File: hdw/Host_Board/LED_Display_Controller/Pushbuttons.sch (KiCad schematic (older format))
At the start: 4 parts

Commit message: Added encoder stuff
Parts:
- added C? (x3): 0.1uF, symbol LED_Display_Local_Library:C_Custom
- added R? (x2): 10k, symbol LED_Display_Local_Library:R_Custom
- added R? (x2): 1k, symbol LED_Display_Local_Library:R_Custom
- added U?: 74LVC2G14, TO_SOT_Packages_SMD:SOT-363_SC-70-6, symbol LED_Display_Local_Library:74LVC2G14_Power
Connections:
- net +3V3: now also C?.1, R?.1, R?.1
- net GND: now also C?.2, C?.2, C?.2
- net at SW?.A: now also R?.2, R?.2
- net at SW?.B: now also R?.2, R?.2
- new net: C?.1, R?.1 (x2)
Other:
- note removed: "Add flip flop encoder circuit"
- moved on the sheet: R?, SW?, U?

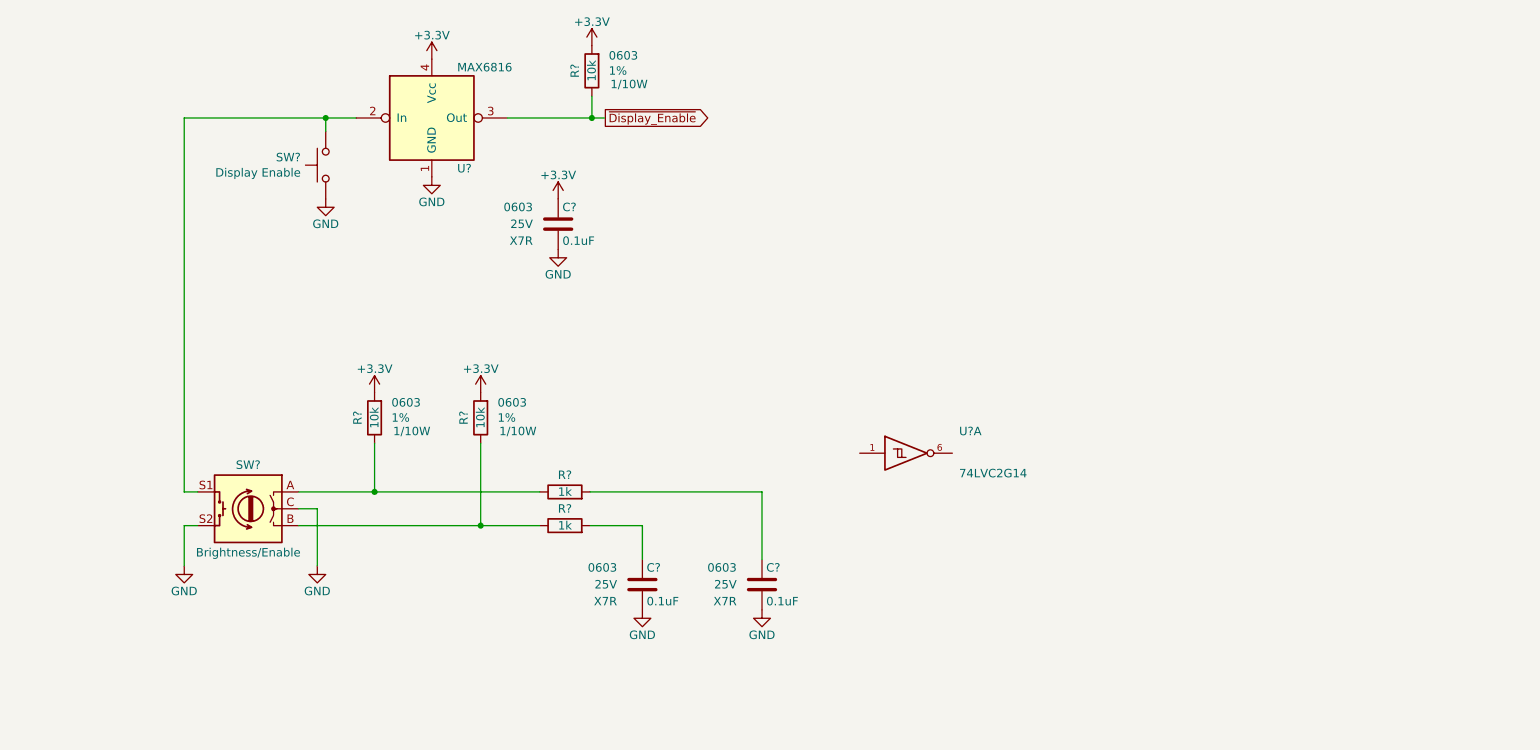
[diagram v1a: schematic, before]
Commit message: revised part numbers in BOM
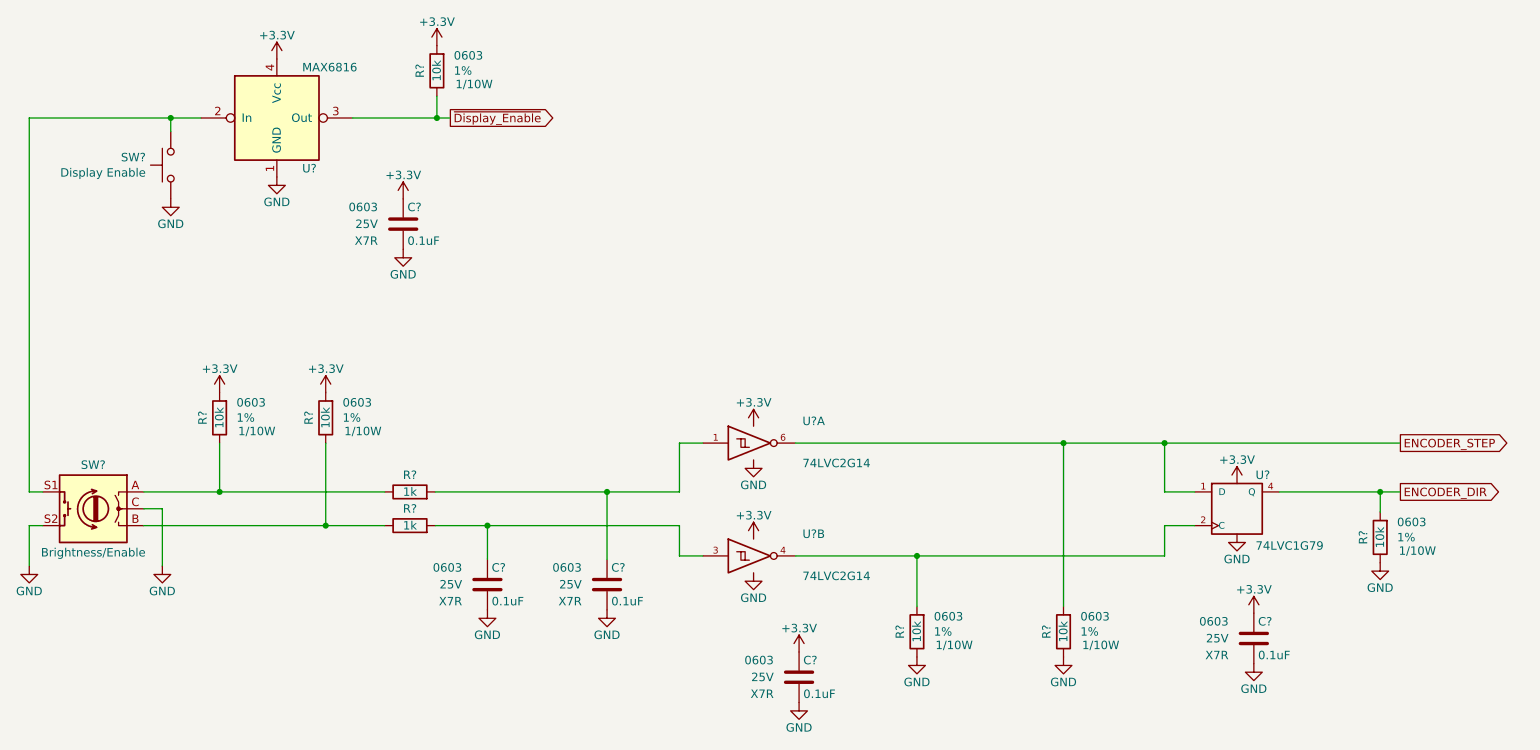
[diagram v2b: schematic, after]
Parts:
- added C? (x2): 0.1uF, symbol LED_Display_Local_Library:C_Custom
- added R? (x3): 10k, symbol LED_Display_Local_Library:R_Custom
- added U?: 74LVC2G14, TO_SOT_Packages_SMD:SOT-363_SC-70-6, symbol LED_Display_Local_Library:74LVC2G14_Power
- added U?: 74LVC1G79, TO_SOT_Packages_SMD:SOT-353_SC-70-5, symbol LED_Display_Local_Library:74LVC1G79_Power
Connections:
- net +3V3: now also U?.5 (VCC), C?.1, C?.1, U?.5 (VCC), U?.5 (VCC)
- net GND: now also U?.2 (GND), C?.2, C?.2, R?.2, R?.2, R?.2, U?.2 (GND), U?.3 (GND)
- net at C?.1, R?.1: now also U?.1
- net at C?.1, R?.1: now also U?.3
- net ENCODER_STEP: now reaches U?.6
- net ENCODER_STEP: now also R?.1, U?.1 (D)
- new net: R?.1, U?.2 (C), U?.4
- new net ENCODER_DIR: R?.1, U?.4 (Q)
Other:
- moved on the sheet: C?, R?, SW?, U?, U?A

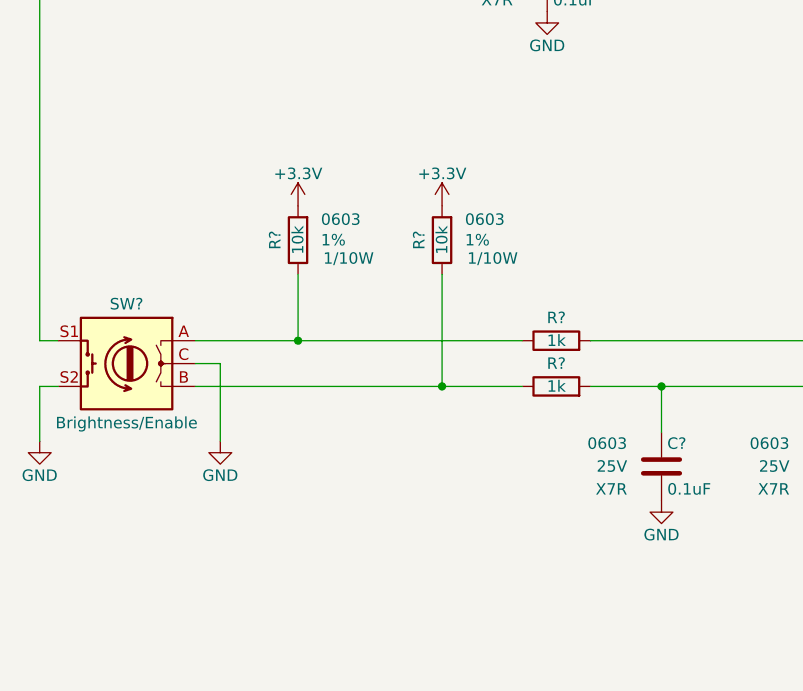
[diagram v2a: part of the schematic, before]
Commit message: Added power board monitoring circuits
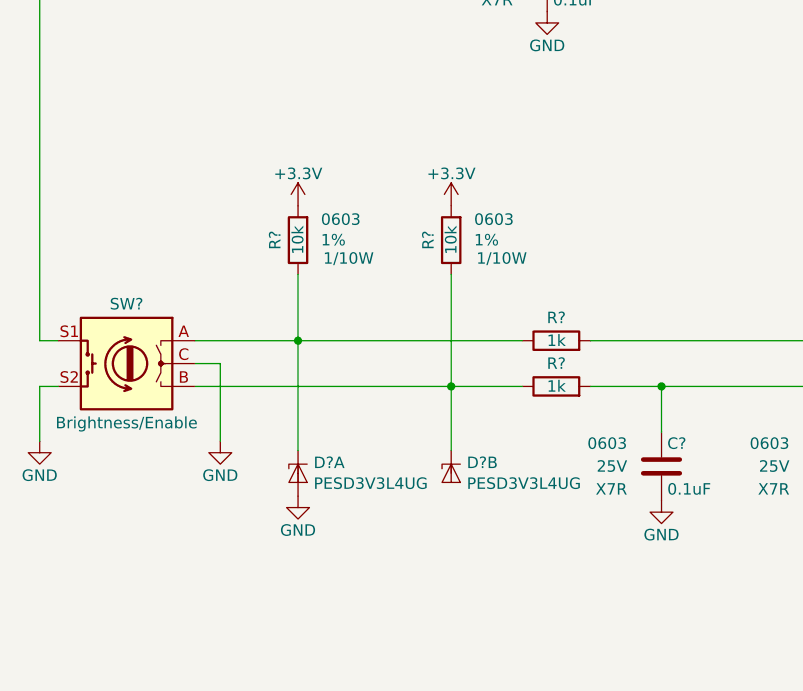
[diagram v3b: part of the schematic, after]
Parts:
- added D? (x2): PESD3V3L4UG, Package_TO_SOT_SMD:SOT-353_SC-70-5, symbol Power_Protection:PESD3V3L4UG
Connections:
- net GND: now also D?.2 (A)
- net at R?.2, R?.2, SW?.A: now also D?.1 (K1)
- net at R?.2, R?.2, SW?.B: now also D?.3 (K2)
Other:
- moved on the sheet: R?
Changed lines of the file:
@@
 L LED_Display_Local_Library:R_Custom R?
 U 1 1 5BE38BE6
-P 2970 3700
-F 0 "R?" V 2870 3700 50  0000 C CNN
-F 1 "10k" V 2970 3700 50  0000 C CNN
-F 2 "" H 2970 3700 50  0001 C CNN
-F 3 "" H 2970 3700 50  0001 C CNN
-F 4 "0603" H 3070 3790 50  0000 L CNN "display_footprint"
-F 5 "1%" H 3070 3700 50  0000 L CNN "Tolerance"
-F 6 "1/10W" H 3080 3620 50  0000 L CNN "Wattage"
-F 7 "PN" H 3270 4100 60  0001 C CNN "Digi-Key PN"
-	1    2970 3700
+P 3010 3700
+F 0 "R?" V 2910 3700 50  0000 C CNN
+F 1 "10k" V 3010 3700 50  0000 C CNN
+F 2 "" H 3010 3700 50  0001 C CNN
+F 3 "" H 3010 3700 50  0001 C CNN
+F 4 "0603" H 3110 3790 50  0000 L CNN "display_footprint"
+F 5 "1%" H 3110 3700 50  0000 L CNN "Tolerance"
+F 6 "1/10W" H 3120 3620 50  0000 L CNN "Wattage"
+F 7 "PN" H 3310 4100 60  0001 C CNN "Digi-Key PN"
+	1    3010 3700
 	1    0    0    -1
 $EndComp
@@
 L power:+3.3V #PWR?
 U 1 1 5BE38BED
-P 2970 3550
-F 0 "#PWR?" H 2970 3400 50  0001 C CNN
-F 1 "+3.3V" H 2970 3690 50  0000 C CNN
-F 2 "" H 2970 3550 50  0001 C CNN
-F 3 "" H 2970 3550 50  0001 C CNN
-	1    2970 3550
+P 3010 3550
+F 0 "#PWR?" H 3010 3400 50  0001 C CNN
+F 1 "+3.3V" H 3010 3690 50  0000 C CNN
+F 2 "" H 3010 3550 50  0001 C CNN
+F 3 "" H 3010 3550 50  0001 C CNN
+	1    3010 3550
 	1    0    0    -1
 $EndComp
@@
 	3320 4140 2340 4140
 Wire Wire Line
-	1890 4340 2970 4340
+	1890 4340 3010 4340
 Wire Wire Line
 	2340 3850 2340 4140
@@
 	2340 4140 1890 4140
 Wire Wire Line
-	2970 3850 2970 4340
-Connection ~ 2970 4340
-Wire Wire Line
-	2970 4340 3320 4340
+	3010 3850 3010 4340
+Connection ~ 3010 4340
+Wire Wire Line
+	3010 4340 3320 4340
 $Comp
 L LED_Display_Local_Library:C_Custom C?
@@
 	9350 3850 7950 3850
 Connection ~ 7950 3850
+$Comp
+L Power_Protection:PESD3V3L4UG D?
+U 1 1 5BF48679
+P 2340 4720
+F 0 "D?" V 2294 4788 50  0000 L CNN
+F 1 "PESD3V3L4UG" V 2385 4788 50  0000 L CNN
+F 2 "Package_TO_SOT_SMD:SOT-353_SC-70-5" H 2340 4720 50  0001 C CNN
+F 3 "http://www.nxp.com/documents/data_sheet/PESDXL4UF_G_W.pdf" H 2340 4720 50  0001 C CNN
+	1    2340 4720
+	0    1    1    0
+$EndComp
+$Comp
+L power:GND #PWR?
+U 1 1 5BF48715
+P 2340 4820
+F 0 "#PWR?" H 2340 4570 50  0001 C CNN
+F 1 "GND" H 2340 4670 50  0000 C CNN
+F 2 "" H 2340 4820 50  0001 C CNN
+F 3 "" H 2340 4820 50  0001 C CNN
+	1    2340 4820
+	1    0    0    -1
+$EndComp
+$Comp
+L Power_Protection:PESD3V3L4UG D?
+U 2 1 5BF4A271
+P 3010 4720
+F 0 "D?" V 2964 4788 50  0000 L CNN
+F 1 "PESD3V3L4UG" V 3055 4788 50  0000 L CNN
+F 2 "Package_TO_SOT_SMD:SOT-353_SC-70-5" H 3010 4720 50  0001 C CNN
+F 3 "http://www.nxp.com/documents/data_sheet/PESDXL4UF_G_W.pdf" H 3010 4720 50  0001 C CNN
+	2    3010 4720
+	0    1    1    0
+$EndComp
+Wire Wire Line
+	3010 4620 3010 4340
+Wire Wire Line
+	2340 4620 2340 4140
 $EndSCHEMATC

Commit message: connected signals to MCU pins
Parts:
- D? (x2): symbol Power_Protection:PESD3V3L4UG -> LED_Display_Controller-rescue:PESD3V3L4UG-Power_Protection
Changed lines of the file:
@@
 Connection ~ 7950 3850
 $Comp
-L Power_Protection:PESD3V3L4UG D?
+L LED_Display_Controller-rescue:PESD3V3L4UG-Power_Protection D?
 U 1 1 5BF48679
 P 2340 4720
@@
 $EndComp
 $Comp
-L Power_Protection:PESD3V3L4UG D?
+L LED_Display_Controller-rescue:PESD3V3L4UG-Power_Protection D?
 U 2 1 5BF4A271
 P 3010 4720
